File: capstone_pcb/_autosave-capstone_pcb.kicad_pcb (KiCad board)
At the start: 2 copper layers, 43 parts, among them IC6 BSS138, P1 MHDR1X5, Q1 BSS138, U2 BMI270, U3 NRF52840-QIAA-R, U4 MAX30102EFD+T, X1 32MHz, X2 32.768kHz

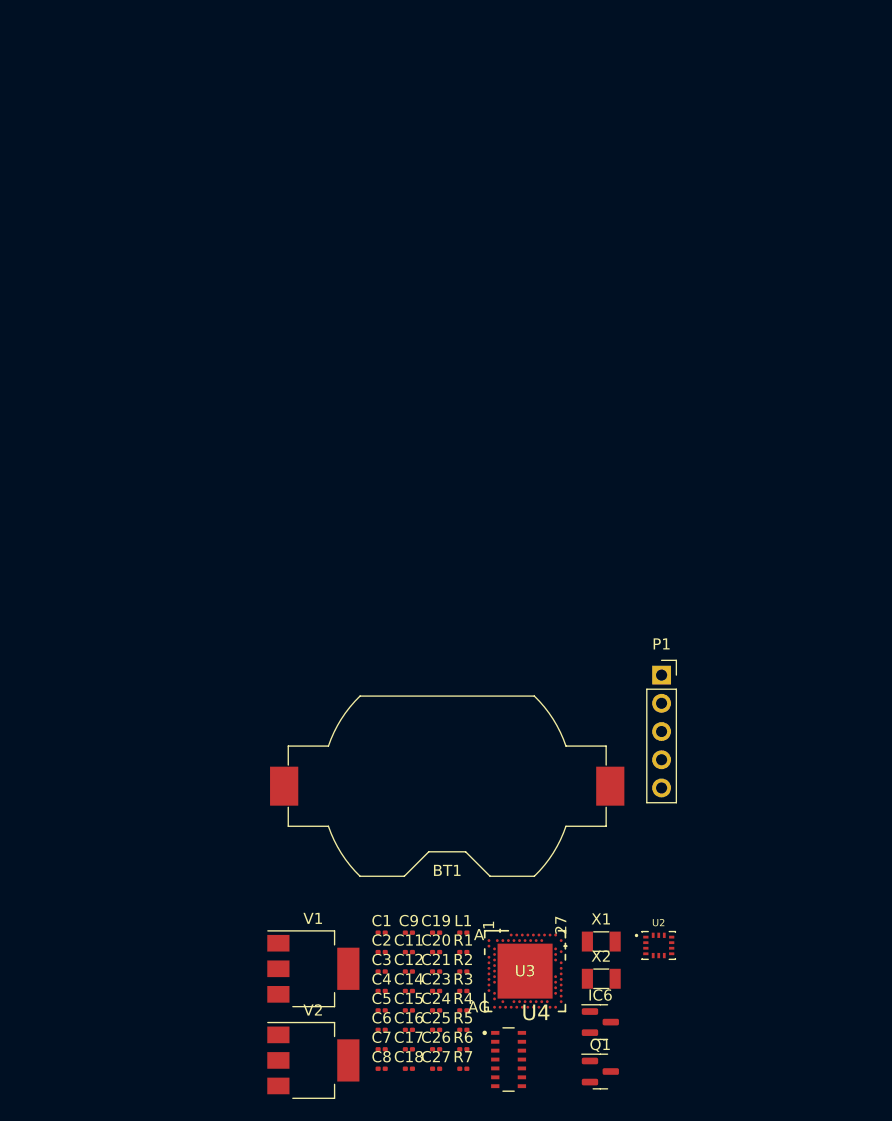
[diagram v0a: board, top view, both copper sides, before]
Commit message: PCB layout complete
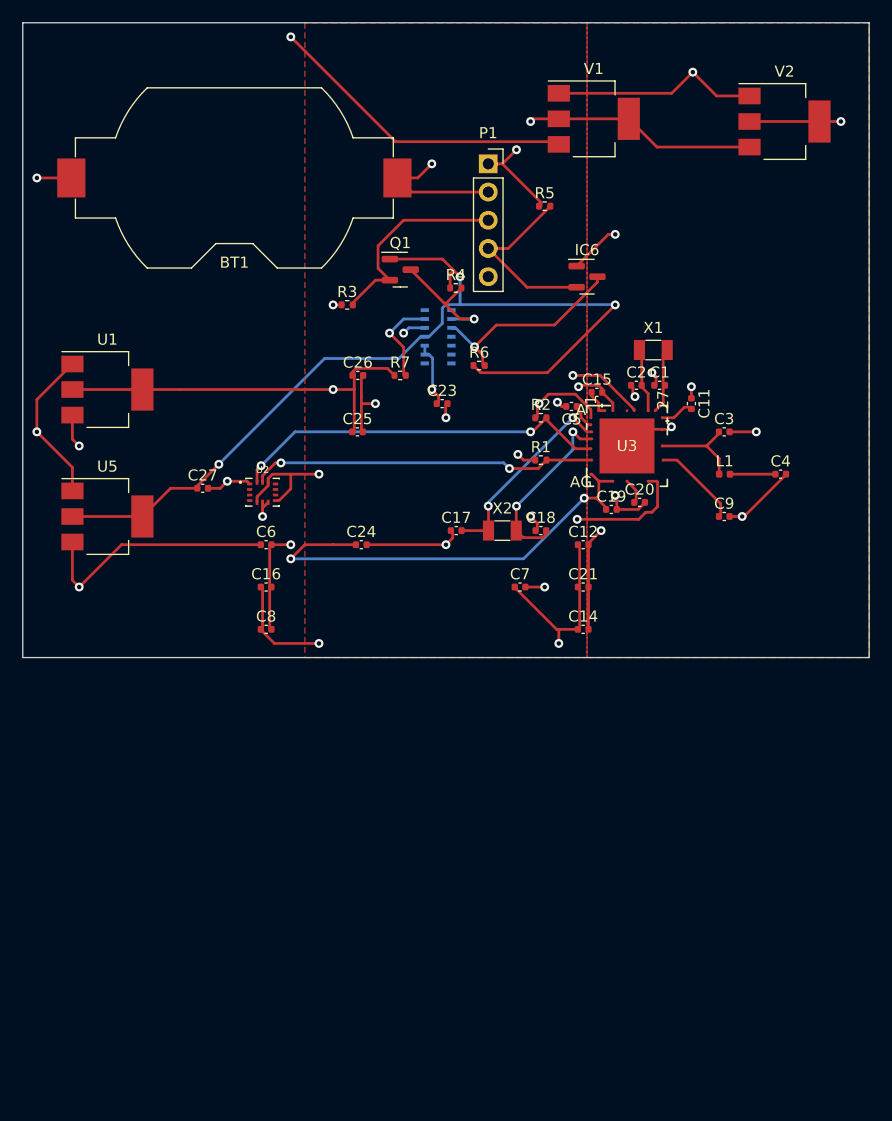
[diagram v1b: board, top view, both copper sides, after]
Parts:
- added U1: AMS1117-3.3, Package_TO_SOT_SMD:SOT-223-3_TabPin2, F.Cu at (83.8, 50.8)
- added U5: AMS1117-1.8, Package_TO_SOT_SMD:SOT-223-3_TabPin2, F.Cu at (83.8, 62.2)
- C1, C11, C12, C14, C15, C16, C17, C18, C19, C2, C20, C21, C23, C24, C25, C26, C27, C3, C4, C5, C6, C7, C8, C9: footprint Capacitor_SMD:C_0201_0603Metric -> Capacitor_SMD:C_0402_1005Metric
- L1: footprint Inductor_SMD:L_0201_0603Metric -> Inductor_SMD:L_0402_1005Metric
- R1, R2, R3, R4, R5, R6, R7: footprint Resistor_SMD:R_0201_0603Metric -> Resistor_SMD:R_0402_1005Metric
- U3: footprint Library:nrf52840_qiaa_r -> nrf:nrf52840_qiaa_r
- U4: moved to B.Cu
- moved V2 94.6 mm to (144.8, 26.7)
- moved V1 80.6 mm to (127.6, 26.4)
- moved R5 74.5 mm to (123.2, 34.3)
- moved Q1 74.4 mm to (110.2, 40.0)
- moved IC6 67.1 mm to (127.0, 40.6)
- moved U4 65.4 mm to (113.6, 46.0), turned to 180 degrees
- moved R4 65.0 mm to (115.2, 41.7)
- moved R7 62.7 mm to (110.2, 49.5)
- moved R3 62.6 mm to (105.4, 43.2)
- moved R6 61.6 mm to (117.3, 48.6)
- moved C26 61.1 mm to (106.4, 49.5)
- moved C4 58.8 mm to (144.4, 58.4)
- moved C15 58.2 mm to (127.9, 51.1)
- moved BT1 58.0 mm to (95.2, 31.8)
- moved C3 57.6 mm to (139.4, 54.6)
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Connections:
- BT1 pad 1: VBAT -> +5V
- C12 pad 1: VDD_nRF -> +3.3V
- C14 pad 1: VDD_nRF -> +3.3V
- C16 pad 1: VDD_nRF -> +3.3V
- C19 pad 1: VBUS -> +5V
- C21 pad 1: VDD_nRF -> +3.3V
- C24 pad 1: AVCC -> +5V
- C25 pad 1: 3.3V -> +3.3V
- C26 pad 1: 3.3V -> +3.3V
- C27 pad 1: 1.8V -> +1.8V
- C6 pad 1: VDD_nRF -> +5V
- C7 pad 1: VDD_nRF -> +3.3V
- C8 pad 1: VDD_nRF -> +3.3V
- IC6 pad 1: 3.3V -> +1.8V
- P1 pad 1: AVCC -> +3.3V
- Q1 pad 1: 3.3V -> +1.8V
- R1 pad 1: VDD_nRF -> +3.3V
- R2 pad 1: VDD_nRF -> +3.3V
- R3 pad 1: AVCC -> +3.3V
- R4 pad 1: 3.3V -> +1.8V
- R5 pad 1: AVCC -> +3.3V
- R6 pad 1: 3.3V -> +1.8V
- U2 pad 12: VDD_nRF -> +3.3V
- U2 pad 5: VDD_nRF -> +3.3V
- U2 pad 8: VDD_nRF -> +3.3V
- U3 pad A22: VDD_nRF -> +3.3V
- U3 pad AD14: VDD_nRF -> +3.3V
- U3 pad AD2: VBUS_nrF -> +5V
- U3 pad AD23: VDD_nRF -> +3.3V
- U3 pad B1: VDD_nRF -> +3.3V
- U3 pad W1: VDD_nRF -> +5V
- U3 pad Y2: VBUS -> +5V
- U4 pad 11: +1V8 -> +1.8V
- V1 pad 2: 3.3V -> +3.3V
- V1 pad 3: AVCC -> +5V
- V2 pad 2: 1.8V -> +1.8V
- V2 pad 3: 3.3V -> +3.3V
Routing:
- net +3.3V: track 0.00 -> 128.5 mm, vias 0 -> 11
- net Earth: track 0.00 -> 120.3 mm, vias 0 -> 22
- net +5V: track 0.00 -> 98.3 mm, vias 0 -> 6
- net +1.8V: track 0.00 -> 97.5 mm, vias 0 -> 5
- net /SDA: track 0.00 -> 34.5 mm, vias 0 -> 2
- net /SCL: track 0.00 -> 31.2 mm, vias 0 -> 2
- net /ASCL: track 0.00 -> 18.9 mm
- net /BSDA: track 0.00 -> 18.7 mm, vias 0 -> 1
- net Net-(U3-P0.00/XL1): track 0.00 -> 18.1 mm, vias 0 -> 2
- net Net-(U3-P0.01/XL2): track 0.00 -> 16.6 mm, vias 0 -> 2
- net /ASDA: track 0.00 -> 16.5 mm
- net /BSCL: track 0.00 -> 11.7 mm, vias 0 -> 1
- net Net-(U3-ANT): track 0.00 -> 8.73 mm
- net Net-(U4-*INT): track 0.00 -> 8.04 mm, vias 0 -> 1
- net Net-(U3-DEC5): track 0.00 -> 7.96 mm
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- added copper zone on F.Cu, net +1.8V
- added copper zone on F.Cu, net +3.3V
- added copper zone on In2.Cu, net +5V
- added copper zone on In1.Cu, net Earth
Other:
- board outline added: 76.2 x 57.2 mm
- copper layers 2 -> 4
